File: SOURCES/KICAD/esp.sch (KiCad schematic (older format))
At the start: 14 parts, among them IC501 ESP32-WROOM-32U, Q501 Q_SS8050-G, Q502 Q_SS8050-G, SW501 SW_Push, X501 Conn_01x04, X502 Conn_01x05, X503 Conn_01x03, X504 HDR_01x06

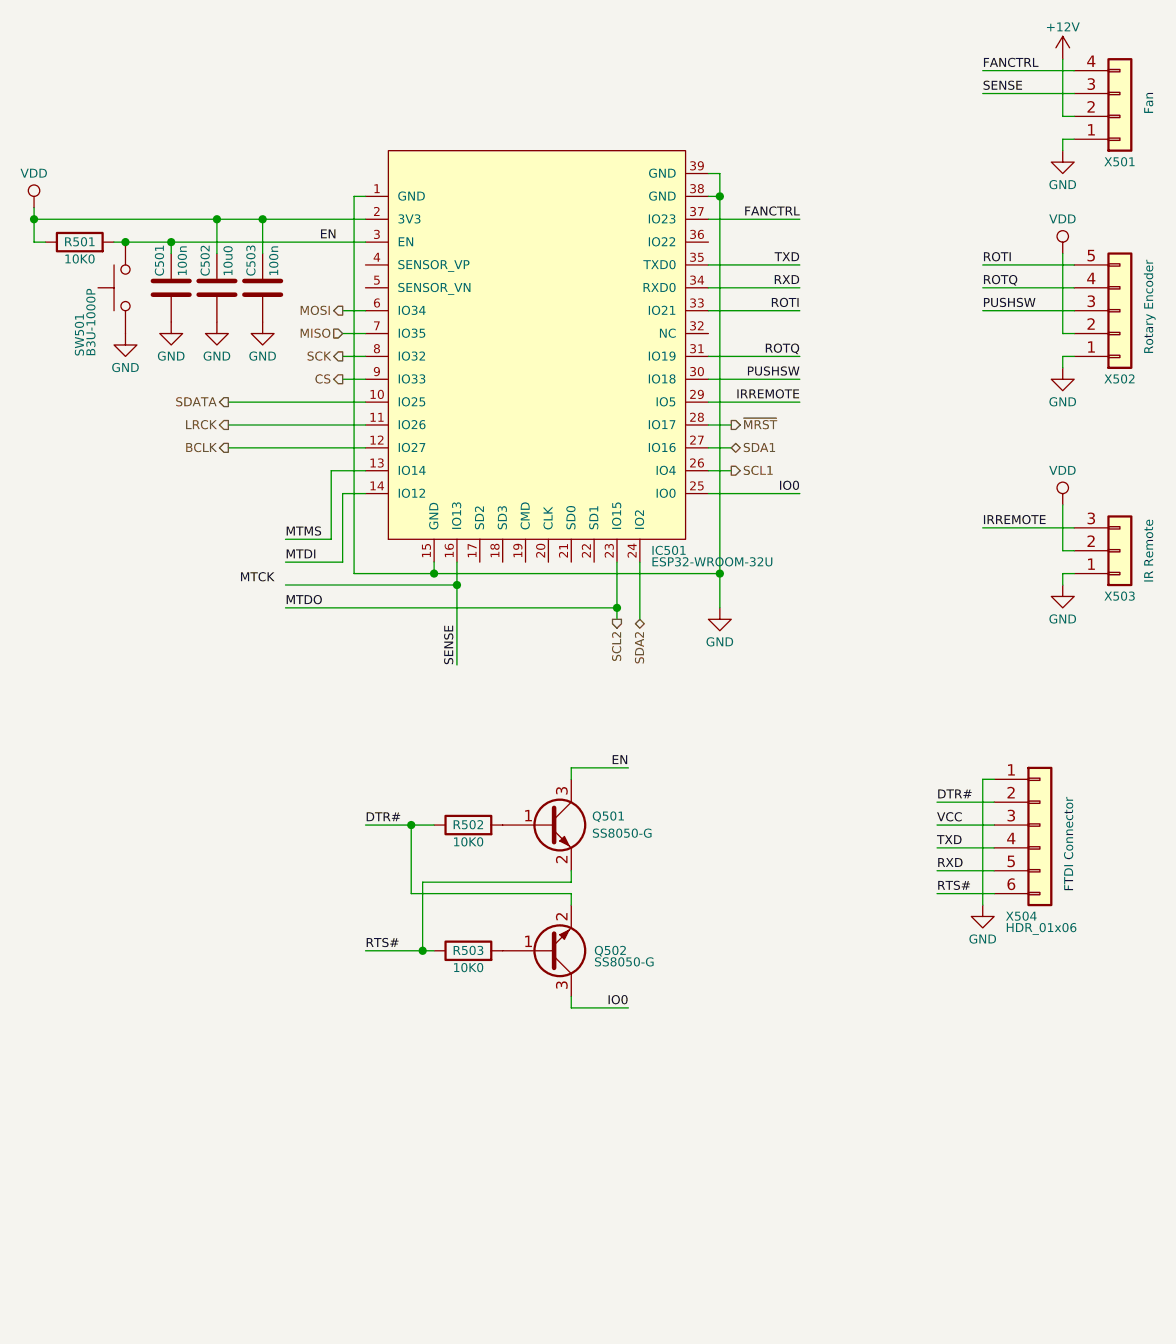
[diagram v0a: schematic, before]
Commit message: Updated sendParameter
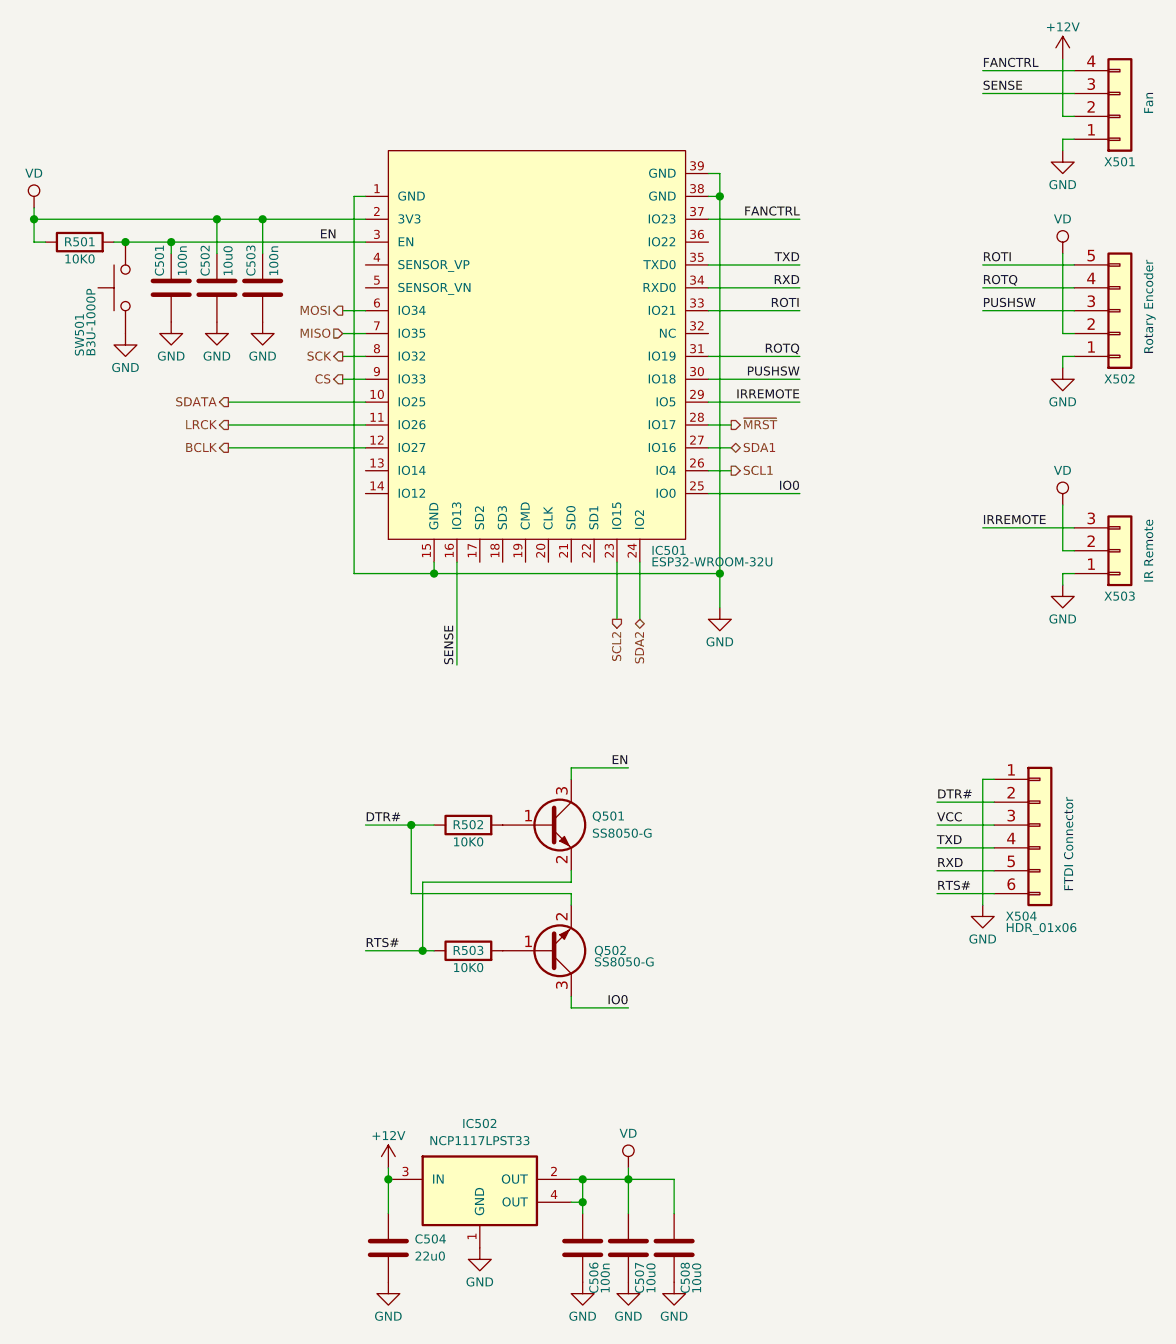
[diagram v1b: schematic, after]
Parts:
- added C504: CAP_22u0_10V_X5R_0805, rklib:C0805-X7R, symbol rk:CAP_22u0_10V_X5R_0805
- added C506: CAP_100n_50V_X7R_0805, rklib:C0805-X7R, symbol rk:CAP_100n_50V_X7R_0805
- added C507, C508: CAP_10u0_25V_X5R_0805, rklib:C0805-X7R, symbol rk:CAP_10u0_25V_X5R_0805
- added IC502: IC_NCP1117LPST33, rklib:SOT223, symbol rk:IC_NCP1117LPST33
- Q501, Q502: digikey ??? -> 641-1790-1-ND
- X501: digikey ??? -> WM4202-ND
- X502: digikey ??? -> WM1734-ND
- X503: digikey ??? -> WM1732-ND
- X504: digikey ??? -> S1011EC-06-ND
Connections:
- net +12V: now also C504.1, IC502.3 (IN)
- net GND: now also C504.2, C506.2, C507.2, C508.2, IC502.1 (GND)
- net MTDI: no longer names the net of IC501.14 (IO12)
- net MTMS: no longer names the net of IC501.13 (IO14)
- net VDD renamed VD
- net VD: now also C506.1, C507.1, C508.1, IC502.2 (OUT), IC502.4 (OUT)
